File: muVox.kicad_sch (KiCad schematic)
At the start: 57 parts, among them J1 STEMMA QT, J2 JTAG_EXTRA, J3 Programmer, J4 Alt.DC, J5 DC IN, SW1 EG120A, U1 TPS5430DDA, U2 ZD24C08AE1, U3 XC6220B331MR

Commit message: fix: incorrect subschematic path
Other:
- sheet Amplifier #0: file ext_Sch/MA12070P.kicad_sch -> ./ext_sch/MA12070P.kicad_sch
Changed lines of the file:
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@@
       (effects (font (size 1.27 1.27)) (justify left bottom))
     )
-    (property "Sheet file" "ext_Sch/MA12070P.kicad_sch" (id 1) (at 182.245 92.6596 0)
+    (property "Sheet file" "./ext_sch/MA12070P.kicad_sch" (id 1) (at 182.245 92.6596 0)
       (effects (font (size 1.27 1.27)) (justify left top) hide)
     )
@@
       (reference "#PWR058") (unit 1) (value "GND") (footprint "")
     )
+    (path "/e1926d9f-dcd0-4fb0-88d5-346fe5dbea73/00000000-0000-0000-0000-00006044f4b5"
+      (reference "#PWR?") (unit 1) (value "~") (footprint "")
+    )
+    (path "/e1926d9f-dcd0-4fb0-88d5-346fe5dbea73/00000000-0000-0000-0000-00006064c9f1"
+      (reference "#PWR?") (unit 1) (value "~") (footprint "")
+    )
+    (path "/e1926d9f-dcd0-4fb0-88d5-346fe5dbea73/00000000-0000-0000-0000-00006067a410"
+      (reference "#PWR?") (unit 1) (value "~") (footprint "")
+    )
+    (path "/e1926d9f-dcd0-4fb0-88d5-346fe5dbea73/00000000-0000-0000-0000-0000665136e7"
+      (reference "#PWR?") (unit 1) (value "~") (footprint "")
+    )
+    (path "/e1926d9f-dcd0-4fb0-88d5-346fe5dbea73/03e227c7-613d-487a-ad75-65cf2c06d312"
+      (reference "#PWR?") (unit 1) (value "GND") (footprint "")
+    )
+    (path "/e1926d9f-dcd0-4fb0-88d5-346fe5dbea73/063d7ff0-6936-4c1f-88c2-d5afe18b546e"
+      (reference "#PWR?") (unit 1) (value "VCCQ") (footprint "")
+    )
+    (path "/e1926d9f-dcd0-4fb0-88d5-346fe5dbea73/0d0574ff-f863-410d-a183-e458c5506ec5"
+      (reference "#PWR?") (unit 1) (value "VCCQ") (footprint "")
+    )
+    (path "/e1926d9f-dcd0-4fb0-88d5-346fe5dbea73/200dda13-313c-45ba-9b77-1ddd6e739437"
+      (reference "#PWR?") (unit 1) (value "GND") (footprint "")
+    )
+    (path "/e1926d9f-dcd0-4fb0-88d5-346fe5dbea73/2745a23f-d2a9-4bb1-a099-43ba9cdcf470"
+      (reference "#PWR?") (unit 1) (value "GND") (footprint "")
+    )
+    (path "/e1926d9f-dcd0-4fb0-88d5-346fe5dbea73/3cd6499d-e432-495a-af3d-8334ded611de"
+      (reference "#PWR?") (unit 1) (value "GND") (footprint "")
+    )
+    (path "/e1926d9f-dcd0-4fb0-88d5-346fe5dbea73/76842728-9224-404d-a2d0-4d15b22727d7"
+      (reference "#PWR?") (unit 1) (value "VDC") (footprint "")
+    )
     (path "/e1926d9f-dcd0-4fb0-88d5-346fe5dbea73/79c6a0e2-8a34-48b8-97f7-a056b72bc91a"
-      (reference "#PWR059") (unit 1) (value "GND") (footprint "")
+      (reference "#PWR?") (unit 1) (value "GND") (footprint "")
+    )
+    (path "/e1926d9f-dcd0-4fb0-88d5-346fe5dbea73/7a382603-dd82-4b52-b5b1-24893d201f4d"
+      (reference "#PWR?") (unit 1) (value "GND") (footprint "")
+    )
+    (path "/e1926d9f-dcd0-4fb0-88d5-346fe5dbea73/7b33ae90-cc9d-48ff-855a-521b7d7cc1e2"
+      (reference "#PWR?") (unit 1) (value "GND") (footprint "")
+    )
+    (path "/e1926d9f-dcd0-4fb0-88d5-346fe5dbea73/93999d21-c8c8-4c83-9b10-53def485d1fa"
+      (reference "#PWR?") (unit 1) (value "+5V") (footprint "")
+    )
+    (path "/e1926d9f-dcd0-4fb0-88d5-346fe5dbea73/96ece811-be7a-4eb9-972b-f9eb7b50eab4"
+      (reference "#PWR?") (unit 1) (value "GND") (footprint "")
+    )
+    (path "/e1926d9f-dcd0-4fb0-88d5-346fe5dbea73/a8c0ae4d-a103-4ab1-9384-a7d0e8b7b17a"
+      (reference "#PWR?") (unit 1) (value "GND") (footprint "")
+    )
+    (path "/e1926d9f-dcd0-4fb0-88d5-346fe5dbea73/a9ceaa9d-4dd2-464b-986d-0ed2cd0627e9"
+      (reference "#PWR?") (unit 1) (value "GND") (footprint "")
+    )
+    (path "/e1926d9f-dcd0-4fb0-88d5-346fe5dbea73/ab102b24-3ea4-4f0e-bc57-d91b32a56cfc"
+      (reference "#PWR?") (unit 1) (value "VCC") (footprint "")
+    )
+    (path "/e1926d9f-dcd0-4fb0-88d5-346fe5dbea73/ada954bb-22e3-450f-8ba4-90c07c888ca8"
+      (reference "#PWR?") (unit 1) (value "GND") (footprint "")
+    )
+    (path "/e1926d9f-dcd0-4fb0-88d5-346fe5dbea73/c30be4ba-d4ea-48ea-b2fa-8ff6bb6489f4"
+      (reference "#PWR?") (unit 1) (value "GND") (footprint "")
+    )
+    (path "/e1926d9f-dcd0-4fb0-88d5-346fe5dbea73/c42dbba3-b7c3-4995-b405-edae6c9c89cc"
+      (reference "#PWR?") (unit 1) (value "GND") (footprint "")
+    )
+    (path "/e1926d9f-dcd0-4fb0-88d5-346fe5dbea73/c47e8fe9-9e2f-4cfc-a05d-d9c081562191"
+      (reference "#PWR?") (unit 1) (value "GND") (footprint "")
+    )
+    (path "/e1926d9f-dcd0-4fb0-88d5-346fe5dbea73/caba12ca-9cb8-43e2-9514-1911d86d5412"
+      (reference "#PWR?") (unit 1) (value "VCCQ") (footprint "")
+    )
+    (path "/e1926d9f-dcd0-4fb0-88d5-346fe5dbea73/dd96e12a-57e8-4d59-ae30-2024f9d28ead"
+      (reference "#PWR?") (unit 1) (value "VCCQ") (footprint "")
     )
     (path "/e1926d9f-dcd0-4fb0-88d5-346fe5dbea73/ea346fcb-6ecf-4e59-a25b-cb6e5d2b812f"
-      (reference "#PWR060") (unit 1) (value "GND") (footprint "")
-    )
-    (path "/e1926d9f-dcd0-4fb0-88d5-346fe5dbea73/0d0574ff-f863-410d-a183-e458c5506ec5"
-      (reference "#PWR061") (unit 1) (value "VCCQ") (footprint "")
-    )
-    (path "/e1926d9f-dcd0-4fb0-88d5-346fe5dbea73/c47e8fe9-9e2f-4cfc-a05d-d9c081562191"
-      (reference "#PWR062") (unit 1) (value "GND") (footprint "")
-    )
-    (path "/e1926d9f-dcd0-4fb0-88d5-346fe5dbea73/00000000-0000-0000-0000-0000665136e7"
-      (reference "#PWR063") (unit 1) (value "~") (footprint "")
-    )
-    (path "/e1926d9f-dcd0-4fb0-88d5-346fe5dbea73/ada954bb-22e3-450f-8ba4-90c07c888ca8"
-      (reference "#PWR064") (unit 1) (value "GND") (footprint "")
-    )
-    (path "/e1926d9f-dcd0-4fb0-88d5-346fe5dbea73/200dda13-313c-45ba-9b77-1ddd6e739437"
-      (reference "#PWR065") (unit 1) (value "GND") (footprint "")
-    )
-    (path "/e1926d9f-dcd0-4fb0-88d5-346fe5dbea73/a9ceaa9d-4dd2-464b-986d-0ed2cd0627e9"
-      (reference "#PWR066") (unit 1) (value "GND") (footprint "")
-    )
-    (path "/e1926d9f-dcd0-4fb0-88d5-346fe5dbea73/00000000-0000-0000-0000-00006064c9f1"
-      (reference "#PWR067") (unit 1) (value "~") (footprint "")
-    )
-    (path "/e1926d9f-dcd0-4fb0-88d5-346fe5dbea73/03e227c7-613d-487a-ad75-65cf2c06d312"
-      (reference "#PWR068") (unit 1) (value "GND") (footprint "")
-    )
-    (path "/e1926d9f-dcd0-4fb0-88d5-346fe5dbea73/7a382603-dd82-4b52-b5b1-24893d201f4d"
-      (reference "#PWR069") (unit 1) (value "GND") (footprint "")
-    )
-    (path "/e1926d9f-dcd0-4fb0-88d5-346fe5dbea73/93999d21-c8c8-4c83-9b10-53def485d1fa"
-      (reference "#PWR070") (unit 1) (value "+5V") (footprint "")
-    )
-    (path "/e1926d9f-dcd0-4fb0-88d5-346fe5dbea73/c42dbba3-b7c3-4995-b405-edae6c9c89cc"
-      (reference "#PWR071") (unit 1) (value "GND") (footprint "")
-    )
-    (path "/e1926d9f-dcd0-4fb0-88d5-346fe5dbea73/caba12ca-9cb8-43e2-9514-1911d86d5412"
-      (reference "#PWR072") (unit 1) (value "VCCQ") (footprint "")
-    )
-    (path "/e1926d9f-dcd0-4fb0-88d5-346fe5dbea73/96ece811-be7a-4eb9-972b-f9eb7b50eab4"
-      (reference "#PWR073") (unit 1) (value "GND") (footprint "")
-    )
-    (path "/e1926d9f-dcd0-4fb0-88d5-346fe5dbea73/dd96e12a-57e8-4d59-ae30-2024f9d28ead"
-      (reference "#PWR074") (unit 1) (value "VCCQ") (footprint "")
-    )
-    (path "/e1926d9f-dcd0-4fb0-88d5-346fe5dbea73/3cd6499d-e432-495a-af3d-8334ded611de"
-      (reference "#PWR075") (unit 1) (value "GND") (footprint "")
-    )
-    (path "/e1926d9f-dcd0-4fb0-88d5-346fe5dbea73/c30be4ba-d4ea-48ea-b2fa-8ff6bb6489f4"
-      (reference "#PWR076") (unit 1) (value "GND") (footprint "")
+      (reference "#PWR?") (unit 1) (value "GND") (footprint "")
+    )
+    (path "/e1926d9f-dcd0-4fb0-88d5-346fe5dbea73/ec6cfe1d-c061-4e76-962a-90e84064101b"
+      (reference "#PWR?") (unit 1) (value "VCCQ") (footprint "")
+    )
+    (path "/e1926d9f-dcd0-4fb0-88d5-346fe5dbea73/f52149b1-d1d4-4b80-9c05-4c43bfda57d9"
+      (reference "#PWR?") (unit 1) (value "+5V") (footprint "")
     )
     (path "/e1926d9f-dcd0-4fb0-88d5-346fe5dbea73/f9d1a5ea-f9f7-445a-b867-52c6e6669a82"
-      (reference "#PWR077") (unit 1) (value "+5V") (footprint "")
-    )
-    (path "/e1926d9f-dcd0-4fb0-88d5-346fe5dbea73/f52149b1-d1d4-4b80-9c05-4c43bfda57d9"
-      (reference "#PWR078") (unit 1) (value "+5V") (footprint "")
-    )
-    (path "/e1926d9f-dcd0-4fb0-88d5-346fe5dbea73/00000000-0000-0000-0000-00006067a410"
-      (reference "#PWR079") (unit 1) (value "~") (footprint "")
-    )
-    (path "/e1926d9f-dcd0-4fb0-88d5-346fe5dbea73/ec6cfe1d-c061-4e76-962a-90e84064101b"
-      (reference "#PWR080") (unit 1) (value "VCCQ") (footprint "")
-    )
-    (path "/e1926d9f-dcd0-4fb0-88d5-346fe5dbea73/7b33ae90-cc9d-48ff-855a-521b7d7cc1e2"
-      (reference "#PWR081") (unit 1) (value "GND") (footprint "")
-    )
-    (path "/e1926d9f-dcd0-4fb0-88d5-346fe5dbea73/063d7ff0-6936-4c1f-88c2-d5afe18b546e"
-      (reference "#PWR082") (unit 1) (value "VCCQ") (footprint "")
-    )
-    (path "/e1926d9f-dcd0-4fb0-88d5-346fe5dbea73/00000000-0000-0000-0000-00006044f4b5"
-      (reference "#PWR083") (unit 1) (value "~") (footprint "")
-    )
-    (path "/e1926d9f-dcd0-4fb0-88d5-346fe5dbea73/a8c0ae4d-a103-4ab1-9384-a7d0e8b7b17a"
-      (reference "#PWR084") (unit 1) (value "GND") (footprint "")
-    )
-    (path "/e1926d9f-dcd0-4fb0-88d5-346fe5dbea73/76842728-9224-404d-a2d0-4d15b22727d7"
-      (reference "#PWR085") (unit 1) (value "VDC") (footprint "")
-    )
-    (path "/e1926d9f-dcd0-4fb0-88d5-346fe5dbea73/2745a23f-d2a9-4bb1-a099-43ba9cdcf470"
-      (reference "#PWR086") (unit 1) (value "GND") (footprint "")
-    )
-    (path "/e1926d9f-dcd0-4fb0-88d5-346fe5dbea73/ab102b24-3ea4-4f0e-bc57-d91b32a56cfc"
-      (reference "#PWR087") (unit 1) (value "VCC") (footprint "")
+      (reference "#PWR?") (unit 1) (value "+5V") (footprint "")
     )
     (path "/f61aa6e3-901d-47bd-8af8-6856cee37383"

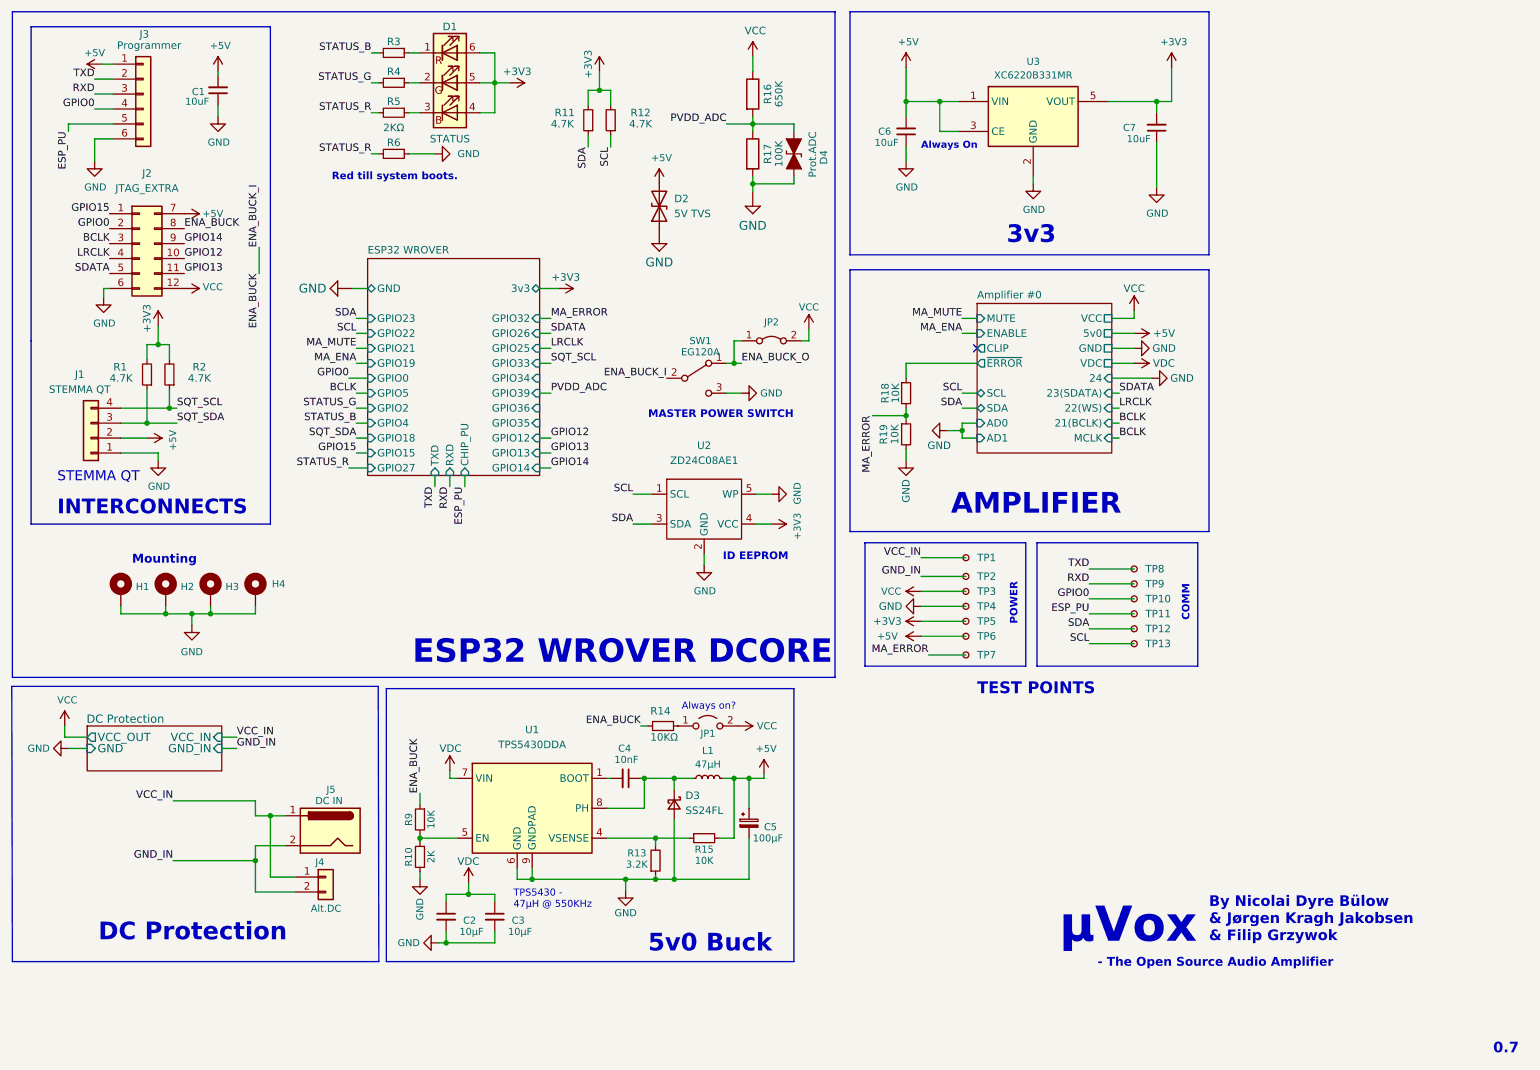
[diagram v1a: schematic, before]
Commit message: Rerouted a couple of small things pr. @feelfreelinux request
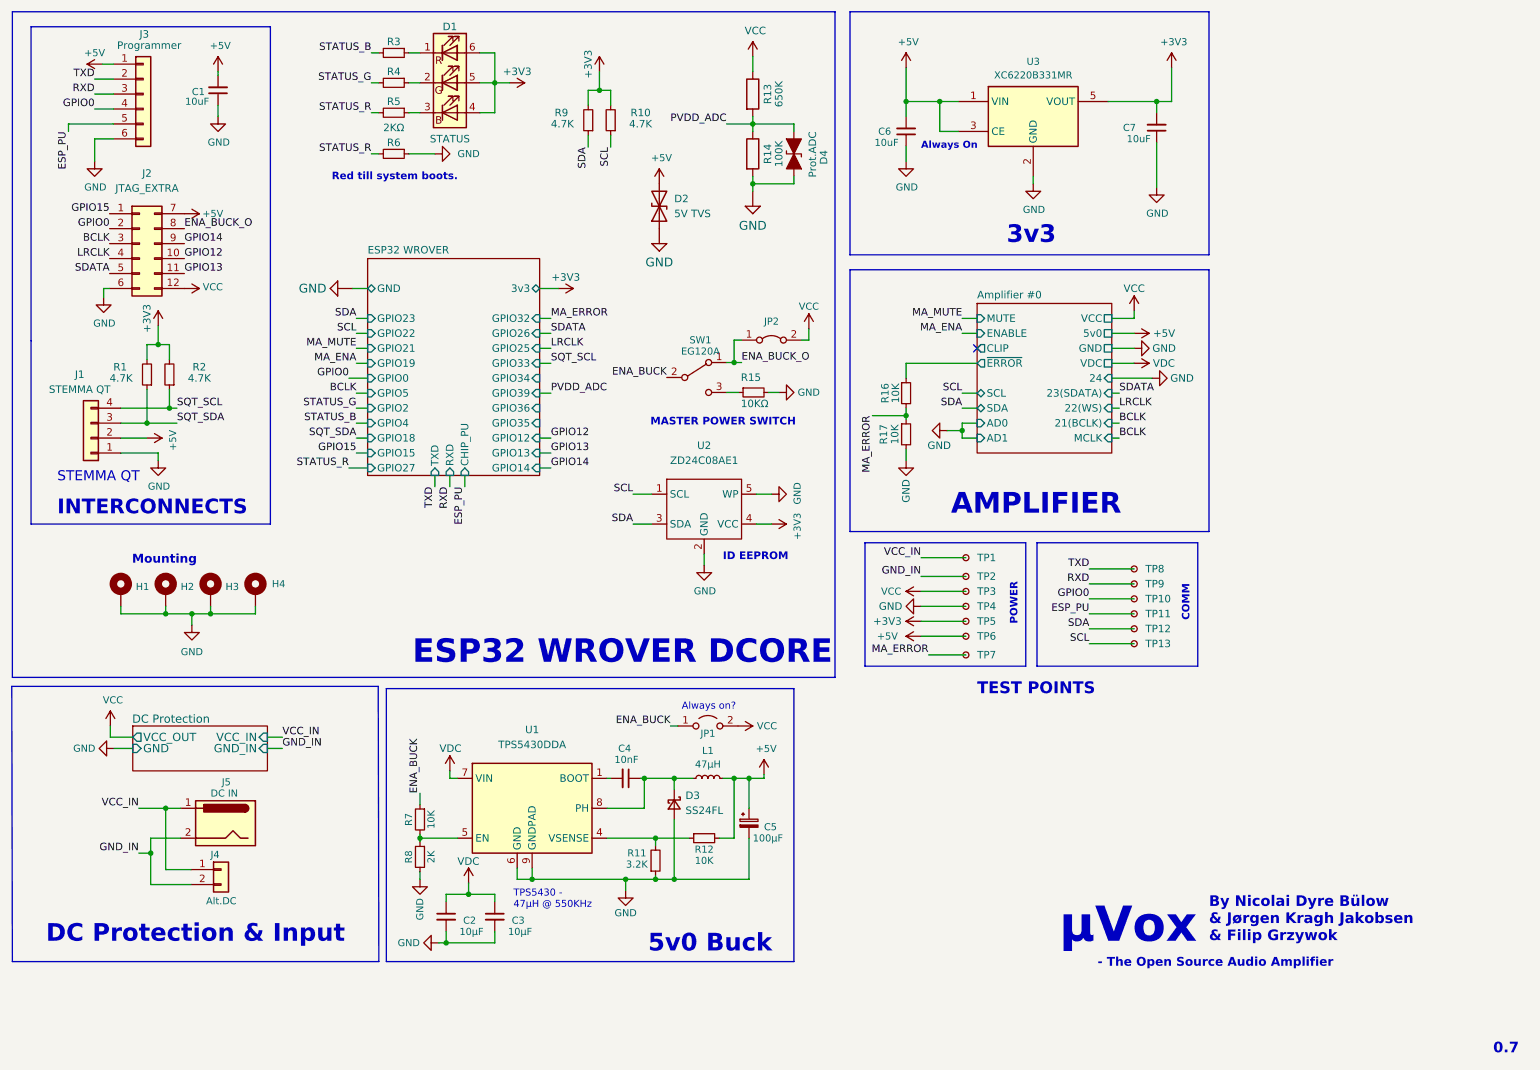
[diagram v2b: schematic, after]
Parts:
- removed R14: 10KΩ, Resistor_SMD:R_0603_1608Metric, symbol Device:R_Small
- added R15: 10KΩ, Resistor_SMD:R_0603_1608Metric, symbol Device:R_Small
- renumbered R12 to R10, R13 to R11, R15 to R12, R16 to R13, R17 to R14, R18 to R16, R19 to R17, R9 to R7, R10 to R8, R11 to R9
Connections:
- net ENA_BUCK: now also JP1.1 (A); no longer J2.8 (Pin_8)
- net ENA_BUCK_O: now also J2.8 (Pin_8)
- net GND: now also R15.2; no longer SW1.3 (C)
- new net: R15.1, SW1.3 (C)
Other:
- note added: "DC Protection & Input"
- note removed: "DC Protection"
- moved on the sheet: J4, J5

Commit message: Small cosmetic changes to both PCB and SCH
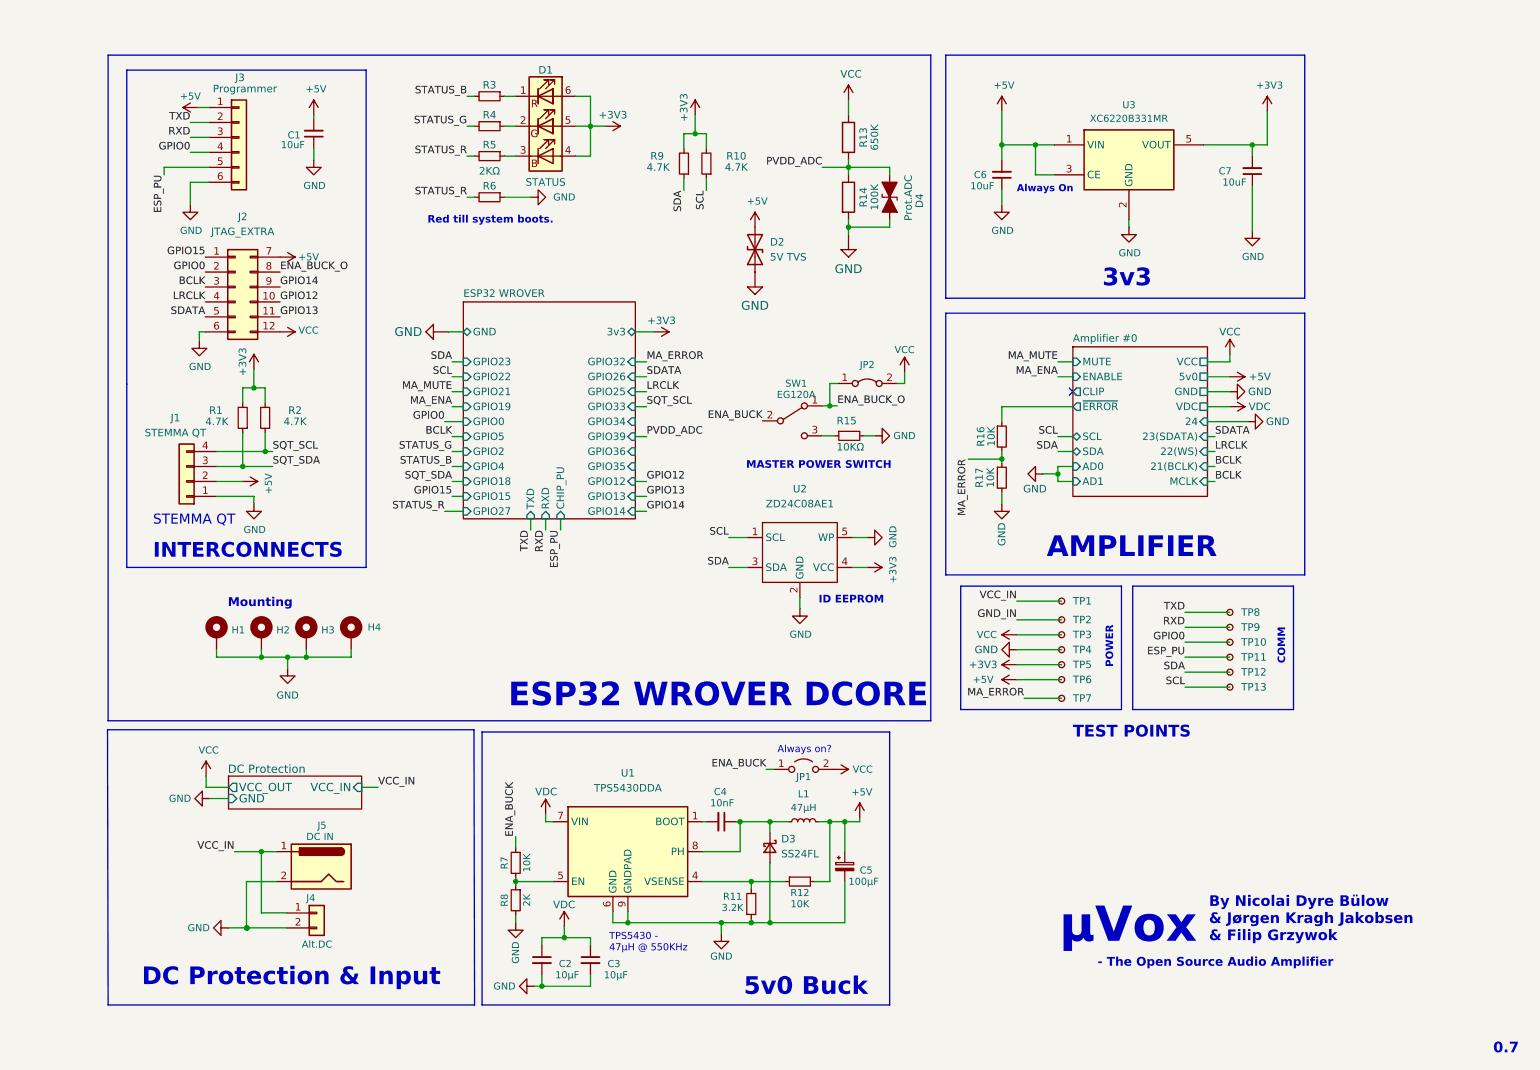
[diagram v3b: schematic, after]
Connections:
- net GND: now also J4.2 (Pin_2), J5.2
- net GND_IN: no longer J4.2 (Pin_2), J5.2
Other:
- sheet DC Protection ports: added none; removed GND_IN
- moved on the sheet: C1, C2, C3, C4, C5, C6, C7, D1, D2, D3, D4, H1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
